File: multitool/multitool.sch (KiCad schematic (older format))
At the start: 86 parts, among them J1 USB, J14 WS2813, J15 ESP-01, J16 VDDS, J17 MNT, J18 MNT, J19 MNT, J2 SELF_PGM, J20 MNT, J3 UNIVERSAL, J4 WSOUT, J5 VPPS, J6 SAO, J7 VDDS, J8 PADAUK, J9 AVR, Q1 3402, Q2 3402, Q3 3402, Q4 3402, Q5 Q_PNP_BEC, SW1 BOOT0, SW2 SUBCFG, U1 STM32F042, U2 MT2492, U3 NUP4202, U4 XC6206P360MR, U5 SP485, U6 INA181A3, U7 74LVC02APW, U8 LOADSW, U9 LOADSW

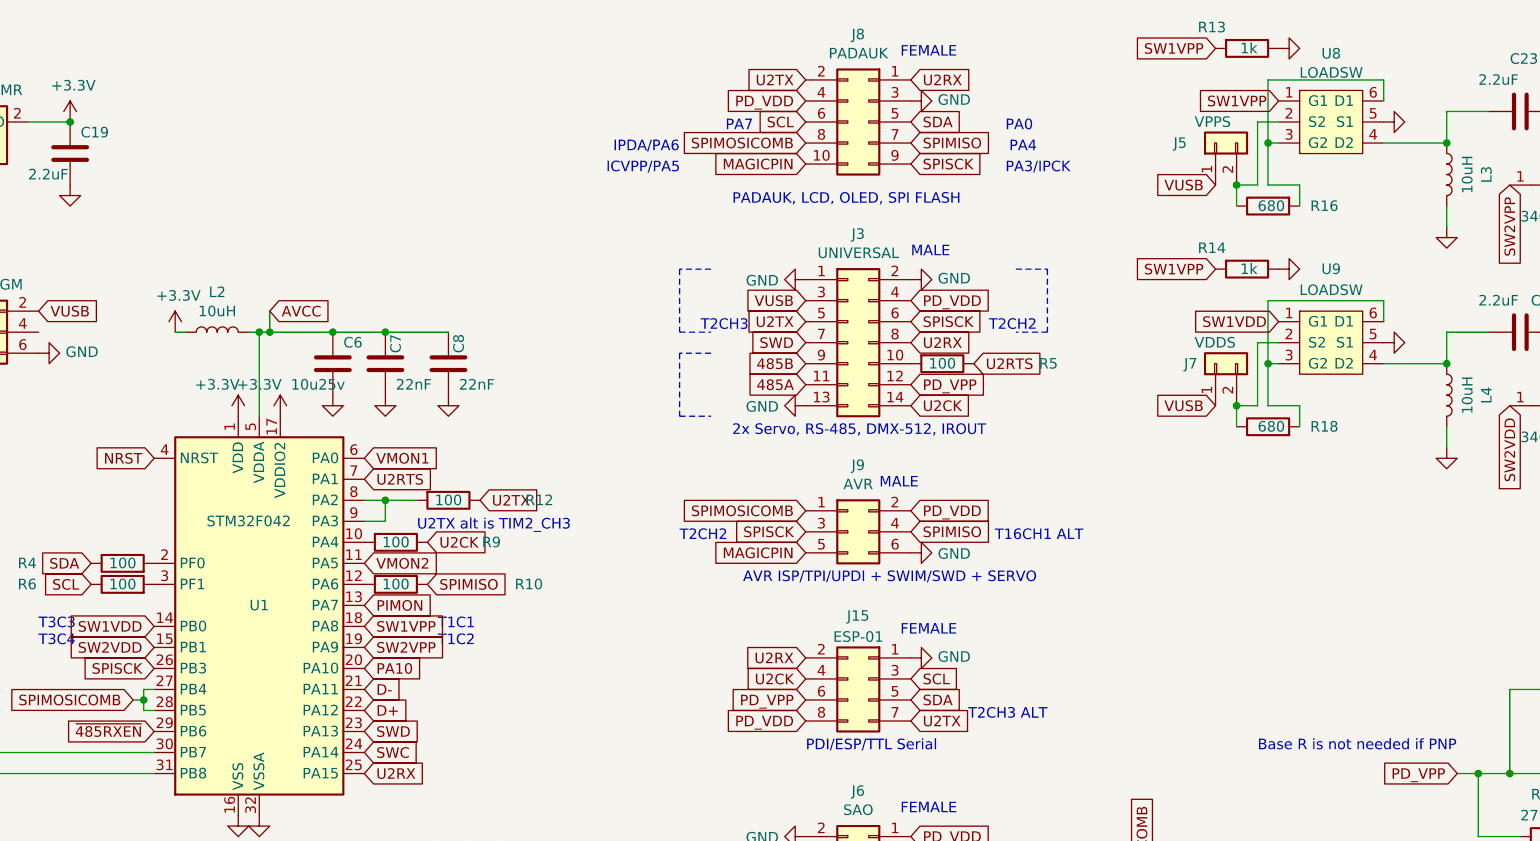
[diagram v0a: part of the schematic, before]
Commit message: Bump design - showing the 5V Vusb monitor
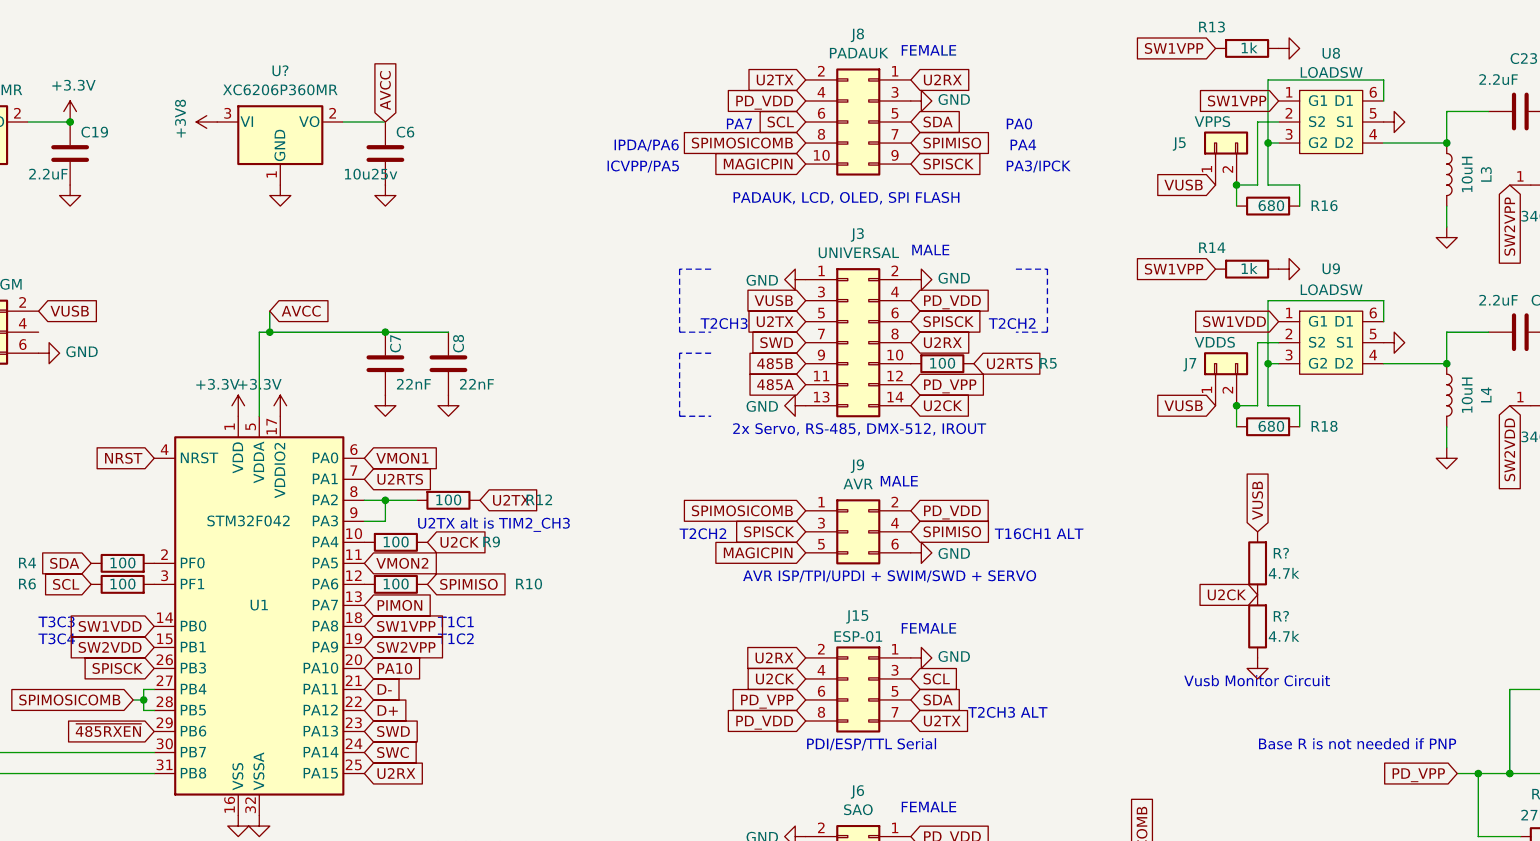
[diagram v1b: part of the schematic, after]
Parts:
- removed L2: 10uH, Inductor_SMD:L_2816_7142Metric, symbol multitool-rescue:L-Device-tensigral_lamp_hardware-rescue-tensigral_lamp_hardwar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
- added R? (x2): 4.7k, Resistor_SMD:R_0603_1608Metric, symbol multitool-rescue:R-Device-tensigral_lamp_hardware-rescue-tensigral_lamp_hardwar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
- added U?: XC6206P360MR, Package_TO_SOT_SMD:SOT-23, symbol Regulator_Linear:XC6206PxxxMR
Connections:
- net +3V8: now also U?.3 (VI)
- net AVCC: now also U?.2 (VO)
- net GND: now also R?.1, U?.1 (GND)
- net U2CK: now also R?.1, R?.2
- net VUSB: now also R?.2
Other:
- note added: "Vusb Monitor Circuit"
- moved on the sheet: C6
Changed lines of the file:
@@
 $EndComp
 Connection ~ 1700 1050
-$Comp
-L power:+3.3V #PWR0169
-U 1 1 5EDB9A01
-P 2200 2050
-F 0 "#PWR0169" H 2200 1900 50  0001 C CNN
-F 1 "+3.3V" H 2215 2223 50  0000 C CNN
-F 2 "" H 2200 2050 50  0001 C CNN
-F 3 "" H 2200 2050 50  0001 C CNN
-	1    2200 2050
-	1    0    0    -1
-$EndComp
 Wire Wire Line
 	2600 2450 2600 2050
 Wire Wire Line
 	2600 2050 2650 2050
-$Comp
-L multitool-rescue:GND-power-tensigral_lamp_hardware-rescue-tensigral_lamp_hardware-rescue #PWR0170
-U 1 1 5EDBE780
-P 2950 2350
-F 0 "#PWR0170" H 2950 2100 50  0001 C CNN
-F 1 "GND" V 2955 2222 50  0001 R CNN
-F 2 "" H 2950 2350 50  0001 C CNN
-F 3 "" H 2950 2350 50  0001 C CNN
-	1    2950 2350
-	1    0    0    -1
-$EndComp
 $Comp
 L power:+3.3V #PWR0171
@@
 $EndComp
 $Comp
-L multitool-rescue:L-Device-tensigral_lamp_hardware-rescue-tensigral_lamp_hardware-rescue L2
-U 1 1 5EDC349F
-P 2400 2050
-F 0 "L2" V 2590 2050 50  0000 C CNN
-F 1 "10uH" V 2499 2050 50  0000 C CNN
-F 2 "Inductor_SMD:L_2816_7142Metric" H 2400 2050 50  0001 C CNN
-F 3 "~" H 2400 2050 50  0001 C CNN
-F 4 "https://lcsc.com/product-detail/New-Arrivals_YJYCOIN-CD32YP0302-100M_C492261.html" V 2400 2050 50  0001 C CNN "LCSC"
-F 5 "0.028838" V 2400 2050 50  0001 C CNN "Cost100"
-	1    2400 2050
-	0    -1   -1   0
-$EndComp
-$Comp
 L multitool-rescue:GND-power-tensigral_lamp_hardware-rescue-tensigral_lamp_hardware-rescue #PWR0172
 U 1 1 5EDC8D21
@@
 	1    0    0    -1
 $EndComp
-Connection ~ 2600 2050
 $Comp
 L Power_Protection:NUP4202 U3
@@
 Text GLabel 8550 1350 3    50   Input ~ 0
 SW2VPP
-Wire Wire Line
-	2600 2050 2550 2050
-Wire Wire Line
-	2250 2050 2200 2050
 $Comp
 L multitool-rescue:R-Device-tensigral_lamp_hardware-rescue-tensigral_lamp_hardware-rescue R6
@@
 L multitool-rescue:C-Device-tensigral_lamp_hardware-rescue-tensigral_lamp_hardware-rescue C6
 U 1 1 5F3688D7
-P 2950 2200
-F 0 "C6" H 3000 2300 50  0000 L CNN
-F 1 "10u25v" H 2750 2100 50  0000 L CNN
-F 2 "Capacitor_SMD:C_0805_2012Metric_Pad1.15x1.40mm_HandSolder" H 2988 2050 50  0001 C CNN
-F 3 "~" H 2950 2200 50  0001 C CNN
-F 4 "https://lcsc.com/product-detail/New-Arrivals_Taiyo-Yuden-TMK212BBJ106KG-T_C386085.html" H 2950 2200 50  0001 C CNN "LCSC"
-F 5 "0.017645" H 2950 2200 50  0001 C CNN "Cost100"
-	1    2950 2200
-	1    0    0    -1
-$EndComp
-Connection ~ 2950 2050
-Wire Wire Line
-	2950 2050 3200 2050
+P 3200 1200
+F 0 "C6" H 3250 1300 50  0000 L CNN
+F 1 "10u25v" H 3000 1100 50  0000 L CNN
+F 2 "Capacitor_SMD:C_0805_2012Metric_Pad1.15x1.40mm_HandSolder" H 3238 1050 50  0001 C CNN
+F 3 "~" H 3200 1200 50  0001 C CNN
+F 4 "https://lcsc.com/product-detail/New-Arrivals_Taiyo-Yuden-TMK212BBJ106KG-T_C386085.html" H 3200 1200 50  0001 C CNN "LCSC"
+F 5 "0.017645" H 3200 1200 50  0001 C CNN "Cost100"
+	1    3200 1200
+	1    0    0    -1
+$EndComp
 $Comp
 L multitool-rescue:C-Device-tensigral_lamp_hardware-rescue-tensigral_lamp_hardware-rescue C4
@@
 	1100 3500 1100 4050
 Connection ~ 2650 2050
-Wire Wire Line
-	2650 2050 2950 2050
 Text GLabel 5200 2100 0    50   Input ~ 0
 SWD
@@
 Text GLabel 5700 2400 2    50   Input ~ 0
 U2CK
+Text GLabel 7350 3300 0    50   Input ~ 0
+U2CK
+Text GLabel 7350 3000 1    50   Input ~ 0
+VUSB
+$Comp
+L multitool-rescue:GND-power-tensigral_lamp_hardware-rescue-tensigral_lamp_hardware-rescue #PWR?
+U 1 1 5ED9AC0E
+P 7350 3600
+F 0 "#PWR?" H 7350 3350 50  0001 C CNN
+F 1 "GND" V 7355 3472 50  0001 R CNN
+F 2 "" H 7350 3600 50  0001 C CNN
+F 3 "" H 7350 3600 50  0001 C CNN
+	1    7350 3600
+	1    0    0    -1
+$EndComp
+$Comp
+L multitool-rescue:R-Device-tensigral_lamp_hardware-rescue-tensigral_lamp_hardware-rescue R?
+U 1 1 5ED9DC43
+P 7350 3150
+F 0 "R?" H 7280 3104 50  0000 R CNN
+F 1 "4.7k" H 7300 3200 50  0000 R CNN
+F 2 "Resistor_SMD:R_0603_1608Metric" V 7280 3150 50  0001 C CNN
+F 3 "~" H 7350 3150 50  0001 C CNN
+F 4 "https://lcsc.com/product-detail/Chip-Resistor-Surface-Mount_UNI-ROYAL-Uniroyal-Elec-0603WAF4701T5E_C23162.html" H 7350 3150 50  0001 C CNN "LCSC"
+F 5 "0.002" H 7350 3150 50  0001 C CNN "Cost100"
+	1    7350 3150
+	-1   0    0    1
+$EndComp
+$Comp
+L multitool-rescue:R-Device-tensigral_lamp_hardware-rescue-tensigral_lamp_hardware-rescue R?
+U 1 1 5EDA5076
+P 7350 3450
+F 0 "R?" H 7280 3404 50  0000 R CNN
+F 1 "4.7k" H 7300 3500 50  0000 R CNN
+F 2 "Resistor_SMD:R_0603_1608Metric" V 7280 3450 50  0001 C CNN
+F 3 "~" H 7350 3450 50  0001 C CNN
+F 4 "https://lcsc.com/product-detail/Chip-Resistor-Surface-Mount_UNI-ROYAL-Uniroyal-Elec-0603WAF4701T5E_C23162.html" H 7350 3450 50  0001 C CNN "LCSC"
+F 5 "0.002" H 7350 3450 50  0001 C CNN "Cost100"
+	1    7350 3450
+	-1   0    0    1
+$EndComp
+$Comp
+L Regulator_Linear:XC6206PxxxMR U?
+U 1 1 5EDB2368
+P 2700 1050
+F 0 "U?" H 2700 1292 50  0000 C CNN
+F 1 "XC6206P360MR" H 2700 1201 50  0000 C CNN
+F 2 "Package_TO_SOT_SMD:SOT-23" H 2700 1275 50  0001 C CIN
+F 3 "https://www.torexsemi.com/file/xc6206/XC6206.pdf" H 2700 1050 50  0001 C CNN
+F 4 "https://lcsc.com/product-detail/Low-Dropout-Regulators-LDO_UMW-Youtai-Semiconductor-Co-Ltd-XC6206P362MR_C351446.html" H 2700 1050 50  0001 C CNN "LCSC"
+F 5 "0.017802" H 2700 1050 50  0001 C CNN "Cost100"
+	1    2700 1050
+	1    0    0    -1
+$EndComp
+$Comp
+L multitool-rescue:+3V8-power-tensigral_lamp_hardware-rescue-tensigral_lamp_hardware-rescue #PWR?
+U 1 1 5EDB2376
+P 2400 1050
+F 0 "#PWR?" H 2400 900 50  0001 C CNN
+F 1 "+3V8" H 2415 1223 50  0000 C CNN
+F 2 "" H 2400 1050 50  0001 C CNN
+F 3 "" H 2400 1050 50  0001 C CNN
+	1    2400 1050
+	0    -1   -1   0
+$EndComp
+Wire Wire Line
+	3000 1050 3200 1050
+$Comp
+L multitool-rescue:GND-power-tensigral_lamp_hardware-rescue-tensigral_lamp_hardware-rescue #PWR?
+U 1 1 5EDB237D
+P 2700 1350
+F 0 "#PWR?" H 2700 1100 50  0001 C CNN
+F 1 "GND" V 2705 1222 50  0001 R CNN
+F 2 "" H 2700 1350 50  0001 C CNN
+F 3 "" H 2700 1350 50  0001 C CNN
+	1    2700 1350
+	1    0    0    -1
+$EndComp
+$Comp
+L multitool-rescue:GND-power-tensigral_lamp_hardware-rescue-tensigral_lamp_hardware-rescue #PWR?
+U 1 1 5EDB2383
+P 3200 1350
+F 0 "#PWR?" H 3200 1100 50  0001 C CNN
+F 1 "GND" V 3205 1222 50  0001 R CNN
+F 2 "" H 3200 1350 50  0001 C CNN
+F 3 "" H 3200 1350 50  0001 C CNN
+	1    3200 1350
+	1    0    0    -1
+$EndComp
+Wire Wire Line
+	2650 2050 3200 2050
+Text GLabel 3200 1050 1    50   Input ~ 0
+AVCC
+Text Notes 7000 3750 0    50   ~ 0
+Vusb Monitor Circuit
 $EndSCHEMATC

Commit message: Progress on multitool
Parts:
- added C10, C12: 22nF, Capacitor_SMD:C_0603_1608Metric, symbol multitool-rescue:C-Device-tensigral_lamp_hardware-rescue-tensigral_lamp_hardwar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
- C6: value 10u25v -> 10u
- Q5: value Q_PNP_BEC -> PNP
- R16, R18: value 680 -> 330; footprint Resistor_SMD:R_0805_2012Metric_Pad1.15x1.40mm_HandSolder -> Resistor_SMD:R_0603_1608Metric; Cost100 0.002409 -> 0.002; LCSC https://lcsc.com/product-detail/Chip-Resistor-Surface-Mount_UNI-ROYAL-Uniroyal-Elec-0805W8F6800T5E_C17798.html -> https://lcsc.com/product-detail/Chip-Resistor-Surface-Mount_UNI-ROYAL-Uniroyal-Elec-0603WAF3300T5E_C23138.html
- U10: renamed from U?; value XC6206P360MR -> 3v6
- U4: value XC6206P360MR -> 3v6
- gave numbers to parts that had none: 2
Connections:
- net +3V3: now also C10.2
- net GND: now also C10.1, C12.2
- net PD_VDD: now also R23.1
- net SW1VDD: now also R14.2
- net SW1VPP: no longer R14.2
- net VUSB: now also C12.1
- net at C9.1, L6.2, R17.1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: no longer R23.1
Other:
- note added: "Add line driver to U2RX?"
- note added: "Inductors: https://lcsc.com/product-detail/Power-Inductors_Ceaiya-CR5040-220M_C520354.html (22uH)\nor \nhttps://lcsc.com/product-detail/New-Quadratic-Unclassified-Data_GLE-GCNR4030-100MC_C439346.html (10uH)"
- moved on the sheet: D1, D2, D6, R11, R17, R23, R24, R7, R8, U6

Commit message: bump design slightly.
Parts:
- removed D3: WS2813, LED_SMD:LED_WS2812_PLCC6_5.0x5.0mm_P1.6mm, symbol LED:WS2813
- removed J14: WS2813, Connector_PinHeader_2.54mm:PinHeader_1x04_P2.54mm_Vertical_SMD_Pin1Right, symbol Connector_Generic:Conn_01x04
- added J10: SMARTLED, Connector_PinHeader_2.54mm:PinHeader_1x04_P2.54mm_Vertical_SMD_Pin1Left, symbol Connector_Generic:Conn_01x04
- added U11, U12: 74AHCT1G126, Package_TO_SOT_SMD:SOT-23-6, symbol 74xGxx:74AHCT1G126
- J1: footprint kicad:USBMicroB-U253-051T-4BH89-F1B -> chinese-connectors:chinausb-multi; Cost100 .037085 -> .040037; LCSC https://lcsc.com/product-detail/USB-Connectors_XKB-Enterpri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 -> https://lcsc.com/product-detail/USB-Connectors_Jing-Extensi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
- J15: Cost100 0.94250 -> 0.14; LCSC https://www.digikey.com/product-detail/en/sullins-connector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 -> https://www.aliexpress.com/item/32913377862.html
- J6: Cost100 0.55880 -> .14; LCSC https://www.digikey.com/product-detail/en/harwin-inc/M20-78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 -> https://www.aliexpress.com/item/32913377862.html
- J9: Cost100 0.34500 -> 0.01487; LCSC https://www.digikey.com/product-detail/en/cnc-tech/3020-06-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 -> https://lcsc.com/product-detail/Pin-Header-Female-Header_BO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
- R11, R25, R7, R8: value 1k -> 4.7k; LCSC https://lcsc.com/product-detail/Chip-Resistor-Surface-Mount_UNI-ROYAL-Uniroyal-Elec-0603WAF1001T5E_C21190.html -> https://lcsc.com/product-detail/Chip-Resistor-Surface-Mount_UNI-ROYAL-Uniroyal-Elec-0603WAF4701T5E_C23162.html
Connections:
- net GND: now also R8.1, J10.4 (Pin_4), U11.3 (GND), U12.3 (GND); no longer R8.2
- net MAGICPIN: now also R25.2; no longer R25.1
- net SPIMISO: now also R11.1; no longer R11.2
- net SPIMOSICOMB: now also U11.2; no longer J4.2 (Pin_2)
- net SPISCK: now also U12.2
- net U2RX: now also R25.1, R7.1; no longer R25.2, R7.2
- net VUSB: now also J10.1 (Pin_1)
- net at D6.1 (K): now also R7.2; no longer R11.1
- net at D2.1 (K): now also R8.2; no longer R8.1
- net at D1.1 (K): now also R11.2; no longer R7.1
- net PD_VDD renamed VCC
- net VCC: now also U11.1, U11.5 (VCC), U12.1, U12.5 (VCC)
- new net: J10.3 (Pin_3), J4.2 (Pin_2), U11.4
- new net: J10.2 (Pin_2), U12.4
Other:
- note added: "2x Servo, RS-485, DMX-512, IROUT, ADC"
- note added: "ADC Alt"
- note added: "Allows for slightly different drive voltages."
- note added: "IROUT"
- note removed: "2x Servo, RS-485, DMX-512, IROUT"
- note removed: "Add line driver to U2RX?"
- moved on the sheet: D1, D6, J4, Q3, Q4, Q5, R15, R19, R20

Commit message: bump
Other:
- note added: "PA10 is free?"
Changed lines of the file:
@@
 Text Notes 6150 2400 0    50   ~ 0
 ADC Alt
+Text Notes 3750 3950 0    118  ~ 0
+PA10 is free?
 $EndSCHEMATC

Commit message: bump
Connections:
- net PA10: now also J15.4 (Pin_4)
- net SPIMISO: now also J3.14 (Pin_14)
- net U2CK: no longer J15.4 (Pin_4), J3.14 (Pin_14)
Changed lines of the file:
@@
 U2RX
 Text GLabel 5200 3700 0    50   Input ~ 0
-U2CK
+PA10
 Text GLabel 5200 3800 0    50   Input ~ 0
 PD_VPP
@@
 	0    1    1    0
 $EndComp
-Text GLabel 5700 2400 2    50   Input ~ 0
-U2CK
 Text GLabel 7350 3300 0    50   Input ~ 0
 U2CK
@@
 Text Notes 6700 5800 0    50   ~ 0
 Allows for slightly different drive voltages.
-Text Notes 6150 2400 0    50   ~ 0
+Text Notes 3550 3900 0    118  ~ 0
+PA10 is free?
+Text Notes 6100 2450 0    50   ~ 0
 ADC Alt
-Text Notes 3750 3950 0    118  ~ 0
-PA10 is free?
+Text GLabel 5700 2400 2    50   Input ~ 0
+SPIMISO
 $EndSCHEMATC
